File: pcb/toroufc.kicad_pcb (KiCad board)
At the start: 2 copper layers, 41.9 x 53.7 mm, 73 parts, among them J1 Conn_01x16_Male, J2 Conn_01x16_Male, J3 Conn_01x16_Male, J4 Conn_01x16_Male, J5 Conn_01x16_Male, J6 Conn_01x16_Male, J7 Conn_01x16_Male, J8 Conn_01x16_Male, J9 Conn_01x16_Male

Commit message: Moving stuff.
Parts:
- removed D57, D58, D59, D60, D61, D62, D63, D64: D, Diode_SMD:D_SOD-123
- removed J1, J2: Conn_01x16_Male, Connector_PinHeader_2.54mm:PinHeader_1x16_P2.54mm_Vertical
- added U1: YAAJ_BluePill, bluepill:YAAJ_BluePill_1, F.Cu at (101.0, 71.0)
- J3, J4, J5, J6, J7, J8, J9: moved to F.Cu
- moved D50 1062.6 mm to (116.7, 127.4), turned to 0 degrees
- moved D41 1058.6 mm to (105.2, 127.4), turned to 0 degrees
- moved D56 1056.7 mm to (110.9, 124.0), turned to 0 degrees
- moved D43 1056.7 mm to (110.9, 127.4), turned to 0 degrees
- moved D42 1055.4 mm to (99.4, 124.0), turned to 0 degrees
- moved D48 1050.1 mm to (116.7, 124.0), turned to 0 degrees
- moved D25 1045.3 mm to (128.2, 129.0), turned to 0 degrees
- moved D47 1044.9 mm to (123.6, 119.0), turned to 0 degrees
- moved D54 1043.7 mm to (135.1, 112.2), turned to 0 degrees
- moved D31 1043.5 mm to (99.4, 127.4), turned to 0 degrees
- moved D44 1043.0 mm to (123.6, 115.6), turned to 0 degrees
- moved D28 1042.7 mm to (122.4, 127.4), turned to 0 degrees
- moved D46 1041.5 mm to (129.3, 115.6), turned to 0 degrees
- moved D30 1040.1 mm to (105.2, 124.0), turned to 0 degrees
- moved D45 1038.6 mm to (129.3, 112.2), turned to 0 degrees
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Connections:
- net Net-(D1-Pad1) renamed /ROW8
- net Net-(D10-Pad1) renamed /ROW7
- net Net-(D11-Pad1) renamed /ROW6
- net Net-(D12-Pad1) renamed /ROW5
- net Net-(D13-Pad1) renamed /ROW4
- net Net-(D14-Pad1) renamed /ROW3
- net Net-(D15-Pad1) renamed /ROW2
- net Net-(D16-Pad1) renamed /ROW1
- net Net-(J1-Pad2) renamed /COL1
- net Net-(J1-Pad3) renamed /COL2
- net Net-(J1-Pad4) renamed /COL3
- net Net-(J1-Pad5) renamed /COL4
- net Net-(J1-Pad6) renamed /COL5
- net Net-(J1-Pad7) renamed /COL6
- net Net-(J1-Pad8) renamed /COL7
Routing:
- net Net-(J1-Pad1): track 93.6 -> 0.00 mm, vias 1 -> 0
- net /COL1: track 88.5 -> 0.00 mm, vias 1 -> 0
- net /COL2: track 85.1 -> 0.00 mm, vias 1 -> 0
- net /COL3: track 81.6 -> 0.00 mm, vias 1 -> 0
- net /COL4: track 78.0 -> 0.00 mm, vias 1 -> 0
- net /COL5: track 74.3 -> 0.00 mm, vias 1 -> 0
- net /COL6: track 71.0 -> 0.00 mm, vias 1 -> 0
- net /COL7: track 65.7 -> 0.00 mm
- net /ROW1: track 64.6 -> 0.00 mm
- net /ROW2: track 62.1 -> 0.00 mm
- net /ROW3: track 59.5 -> 0.00 mm
- net /ROW4: track 57.0 -> 0.00 mm
- net /ROW5: track 54.7 -> 0.00 mm
- net /ROW6: track 51.9 -> 0.00 mm
- net /ROW7: track 50.0 -> 0.00 mm
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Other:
- board outline removed
- net class Default removed
- rule pad_to_mask_clearance: 0.051 -> 0

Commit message: Starting with the PCB.
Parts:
- removed D23, D24, D25, D26, D27, D28, D29, D30, D31, D32, D33, D34, D35, D36, D37, D38, D39, D40, D41, D42, D43, D44, D45, D46, D47, D48, D49, D50, D51, D52, D53, D54, D55, D56: D, Diode_SMD:D_SOD-123
- added J1: HAT, Connector_PinHeader_2.54mm:PinHeader_1x06_P2.54mm_Vertical, F.Cu at (66.7, 67.3)
- added J10: RPAD, Connector_PinHeader_2.54mm:PinHeader_1x06_P2.54mm_Vertical, F.Cu at (102.9, 111.8)
- added J11: POT1-3, Connector_PinHeader_2.54mm:PinHeader_1x09_P2.54mm_Vertical, F.Cu at (114.3, 96.5)
- added J12: POT4-6, Connector_PinHeader_2.54mm:PinHeader_1x09_P2.54mm_Vertical, F.Cu at (121.9, 96.5)
- added J13: REN1, Connector_PinHeader_2.54mm:PinHeader_1x05_P2.54mm_Vertical, F.Cu at (78.7, 32.4)
- added J14: REN2, Connector_PinHeader_2.54mm:PinHeader_1x05_P2.54mm_Vertical, F.Cu at (97.2, 32.4)
- added J2: RKR1-2, Connector_PinHeader_2.54mm:PinHeader_1x06_P2.54mm_Vertical, F.Cu at (66.7, 44.5)
- J3: value Conn_01x16_Male -> RKR3-4; footprint Connector_PinHeader_2.54mm:PinHeader_1x16_P2.54mm_Vertical -> Connector_PinHeader_2.54mm:PinHeader_1x06_P2.54mm_Vertical
- J4: value Conn_01x16_Male -> LVR1-2; footprint Connector_PinHeader_2.54mm:PinHeader_1x16_P2.54mm_Vertical -> Connector_PinHeader_2.54mm:PinHeader_1x06_P2.54mm_Vertical
- J5: value Conn_01x16_Male -> MASTER-BIG1; footprint Connector_PinHeader_2.54mm:PinHeader_1x16_P2.54mm_Vertical -> Connector_PinHeader_2.54mm:PinHeader_1x06_P2.54mm_Vertical
- J6: value Conn_01x16_Male -> BIG2-3-4; footprint Connector_PinHeader_2.54mm:PinHeader_1x16_P2.54mm_Vertical -> Connector_PinHeader_2.54mm:PinHeader_1x06_P2.54mm_Vertical
- J7: value Conn_01x16_Male -> NPAD; footprint Connector_PinHeader_2.54mm:PinHeader_1x16_P2.54mm_Vertical -> Connector_PinHeader_2.54mm:PinHeader_1x10_P2.54mm_Vertical
- J8: value Conn_01x16_Male -> HPAD; footprint Connector_PinHeader_2.54mm:PinHeader_1x16_P2.54mm_Vertical -> Connector_PinHeader_2.54mm:PinHeader_1x08_P2.54mm_Vertical
- J9: value Conn_01x16_Male -> LPAD; footprint Connector_PinHeader_2.54mm:PinHeader_1x16_P2.54mm_Vertical -> Connector_PinHeader_2.54mm:PinHeader_1x06_P2.54mm_Vertical
- U1: value YAAJ_BluePill -> BluePill
- moved D19 110.7 mm to (79.4, 102.9), turned to 90 degrees
- moved D18 109.1 mm to (74.3, 102.9), turned to 90 degrees
- moved D20 105.0 mm to (69.2, 92.7), turned to 90 degrees
- moved D14 102.5 mm to (71.8, 59.7), turned to 90 degrees
- moved D1 99.8 mm to (67.9, 72.4), turned to 90 degrees
- moved D9 99.7 mm to (67.9, 82.5), turned to 90 degrees
- moved D16 95.5 mm to (79.4, 59.7), turned to 90 degrees
- moved D7 93.8 mm to (75.6, 49.5), turned to 90 degrees
- moved D3 92.4 mm to (75.6, 72.4), turned to 90 degrees
- moved D5 92.3 mm to (67.9, 49.5), turned to 90 degrees
- moved D2 90.7 mm to (71.8, 72.4), turned to 90 degrees
- moved D10 90.4 mm to (71.8, 82.5), turned to 90 degrees
- moved D6 90.2 mm to (71.8, 49.5), turned to 90 degrees
- moved D12 88.3 mm to (79.4, 82.5), turned to 90 degrees
- moved D8 87.8 mm to (79.4, 49.5), turned to 90 degrees
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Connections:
- D1 pad 1: /ROW8 -> /ROW5
- D10 pad 1: /ROW7 -> /ROW6
- D11 pad 1: /ROW6 -> /ROW7
- D12 pad 1: /ROW5 -> /ROW8
- D13 pad 1: /ROW4 -> /ROW1
- D14 pad 1: /ROW3 -> /ROW2
- D15 pad 1: /ROW2 -> /ROW3
- D16 pad 1: /ROW1 -> /ROW4
- D17 pad 1: /ROW8 -> /ROW6
- D19 pad 1: /ROW6 -> /ROW4
- D2 pad 1: /ROW7 -> /ROW6
- D2 pad 2: Net-(D2-Pad2) -> Net-(J1-Pad3)
- D21 pad 1: /ROW4 -> /ROW6
- D22 pad 1: /ROW3 -> /ROW7
- D3 pad 1: /ROW6 -> /ROW7
- D4 pad 1: /ROW5 -> /ROW8
- D5 pad 1: /ROW4 -> /ROW1
- D6 pad 1: /ROW3 -> /ROW2
- D7 pad 1: /ROW2 -> /ROW3
- D8 pad 1: /ROW1 -> /ROW4
- D9 pad 1: /ROW8 -> /ROW5
- J3 pad 1: Net-(D56-Pad2) -> /COL6
- J3 pad 2: /COL1 -> Net-(D9-Pad2)
- J3 pad 3: Net-(D55-Pad2) -> Net-(D10-Pad2)
- J3 pad 4: /COL1 -> /COL6
- J3 pad 5: Net-(D54-Pad2) -> Net-(D11-Pad2)
- J3 pad 6: /COL1 -> Net-(D12-Pad2)
- J4 pad 1: Net-(D48-Pad2) -> /COL7
- J4 pad 2: /COL2 -> Net-(D13-Pad2)
- J4 pad 3: Net-(D47-Pad2) -> Net-(D14-Pad2)
- J4 pad 4: /COL2 -> /COL7
- J4 pad 5: Net-(D46-Pad2) -> Net-(D15-Pad2)
- J4 pad 6: /COL2 -> Net-(D16-Pad2)
- J5 pad 1: Net-(D40-Pad2) -> /COL5
- J5 pad 2: /COL3 -> Net-(D17-Pad2)
- J5 pad 3: Net-(D39-Pad2) -> /COL5
- J5 pad 4: /COL3 -> Net-(D18-Pad2)
- J5 pad 5: Net-(D38-Pad2) -> /COL3
- J5 pad 6: /COL3 -> Net-(D19-Pad2)
- J6 pad 1: Net-(D32-Pad2) -> /COL3
- J6 pad 2: /COL4 -> Net-(D20-Pad2)
- J6 pad 3: Net-(D31-Pad2) -> /COL3
- J6 pad 4: /COL4 -> Net-(D21-Pad2)
- J6 pad 5: Net-(D30-Pad2) -> /COL3
- J6 pad 6: /COL4 -> Net-(D22-Pad2)
- J7 pad 1: Net-(D24-Pad2) -> /COL2
- J7 pad 10: /COL5 -> /ROW8
- J7 pad 2: /COL5 -> /COL3
- J7 pad 3: Net-(D23-Pad2) -> /ROW1
- J7 pad 4: /COL5 -> /ROW2
- J7 pad 5: Net-(D22-Pad2) -> /ROW3
- J7 pad 6: /COL5 -> /ROW4
- J7 pad 7: Net-(D21-Pad2) -> /ROW5
- J7 pad 8: /COL5 -> /ROW6
- J7 pad 9: Net-(D20-Pad2) -> /ROW7
- J8 pad 1: Net-(D16-Pad2) -> /COL1
- J8 pad 2: /COL6 -> /ROW1
- J8 pad 3: Net-(D15-Pad2) -> /ROW2
- J8 pad 4: /COL6 -> /ROW3
- J8 pad 5: Net-(D14-Pad2) -> /ROW4
- J8 pad 6: /COL6 -> /ROW5
- J8 pad 7: Net-(D13-Pad2) -> /ROW6
- J8 pad 8: /COL6 -> /ROW7
- J9 pad 1: Net-(D8-Pad2) -> /COL4
- J9 pad 2: /COL7 -> /ROW1
- J9 pad 3: Net-(D7-Pad2) -> /ROW2
- J9 pad 4: /COL7 -> /ROW3
- J9 pad 5: Net-(D6-Pad2) -> /ROW4
- J9 pad 6: /COL7 -> /ROW5
- U1 pad 1: unconnected-(U1-Pad1) -> /REN1C
- U1 pad 10: /COL5 -> /COL4
- U1 pad 11: /COL4 -> /COL3
- U1 pad 12: /COL3 -> /COL2
- U1 pad 13: /COL2 -> /COL1
- U1 pad 14: unconnected-(U1-Pad14) -> /SCL
- U1 pad 15: /COL1 -> /SDA
- U1 pad 18: unconnected-(U1-Pad18) -> /Vusb
- U1 pad 19: unconnected-(U1-Pad19) -> GND
- U1 pad 2: unconnected-(U1-Pad2) -> /REN1D
- U1 pad 20: unconnected-(U1-Pad20) -> VCC
- U1 pad 23: unconnected-(U1-Pad23) -> /REN2SW
- U1 pad 24: unconnected-(U1-Pad24) -> /REN1SW
- U1 pad 25: unconnected-(U1-Pad25) -> /POT3
- U1 pad 26: unconnected-(U1-Pad26) -> /POT2
- U1 pad 27: unconnected-(U1-Pad27) -> /POT1
- U1 pad 28: unconnected-(U1-Pad28) -> /POT4
- U1 pad 29: unconnected-(U1-Pad29) -> /POT5
- U1 pad 3: unconnected-(U1-Pad3) -> /REN2C
- U1 pad 30: unconnected-(U1-Pad30) -> /POT6
- U1 pad 38: unconnected-(U1-Pad38) -> VCC
- U1 pad 39: unconnected-(U1-Pad39) -> GND
- U1 pad 4: unconnected-(U1-Pad4) -> /REN2D
- U1 pad 40: unconnected-(U1-Pad40) -> GND
- U1 pad 5: unconnected-(U1-Pad5) -> /COL7
- U1 pad 6: /COL7 -> /COL6
- U1 pad 7: /COL6 -> /COL5
- U1 pad 8: unconnected-(U1-Pad8) -> /USBD-
- U1 pad 9: unconnected-(U1-Pad9) -> /USBD+
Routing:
- net VCC: track 0.00 -> 192.5 mm
- net /ROW3: track 0.00 -> 178.5 mm
- net GND: track 0.00 -> 147.5 mm
- net /ROW5: track 0.00 -> 128.4 mm, vias 0 -> 3
- net /ROW6: track 0.00 -> 124.5 mm
- net /ROW1: track 0.00 -> 123.6 mm, vias 0 -> 2
- net /ROW4: track 0.00 -> 120.5 mm, vias 0 -> 1
- net /COL3: track 0.00 -> 110.6 mm, vias 0 -> 1
- net /COL6: track 0.00 -> 86.0 mm
- net /REN1SW: track 0.00 -> 79.9 mm, vias 0 -> 2
- net /ROW7: track 0.00 -> 72.0 mm
- net /REN2SW: track 0.00 -> 71.0 mm, vias 0 -> 1
- net /ROW2: track 0.00 -> 66.3 mm
- net /ROW8: track 0.00 -> 63.5 mm, vias 0 -> 1
- net /COL4: track 0.00 -> 59.1 mm, vias 0 -> 1
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
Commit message: First PCB that passes DRC
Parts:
- added J15: I2C, Connector_PinHeader_2.54mm:PinHeader_1x04_P2.54mm_Vertical, F.Cu at (95.0, 111.8)
- added J16: Conn_01x04_Male, Connector_PinHeader_2.54mm:PinHeader_1x04_P2.54mm_Vertical, F.Cu at (119.8, 111.8)
- moved J7 43.2 mm to (64.3, 111.7), turned to 90 degrees
- moved J13 39.0 mm to (114.3, 48.4), turned to 0 degrees
- moved J10 37.1 mm to (66.9, 120.8), turned to 90 degrees
- moved J8 36.1 mm to (66.9, 116.4), turned to 90 degrees
- moved J14 29.4 mm to (121.8, 48.4), turned to 0 degrees
- moved J9 15.5 mm to (104.7, 120.8)
- moved D10 0.81 mm to (71.2, 83.2)
- moved D11 0.81 mm to (75.1, 83.2)
- moved D12 0.81 mm to (78.9, 83.2)
- moved D20 0.81 mm to (68.7, 93.3)
- moved D21 0.81 mm to (73.8, 93.3)
- moved D22 0.81 mm to (78.9, 93.3)
- moved J6 0.81 mm to (66.2, 88.3)
- moved D14 0.81 mm to (71.2, 60.3)
- moved D15 0.81 mm to (75.1, 60.3)
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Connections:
- D19 pad 1: /ROW4 -> /ROW5
- D20 pad 1: /ROW5 -> /ROW6
- D21 pad 1: /ROW6 -> /ROW7
- D22 pad 1: /ROW7 -> /ROW8
- U1 pad 31: /ROW1 -> /ROW5
- U1 pad 32: /ROW2 -> /ROW6
- U1 pad 33: /ROW3 -> /ROW4
- U1 pad 34: /ROW4 -> /ROW3
- U1 pad 35: /ROW5 -> /ROW2
- U1 pad 36: /ROW6 -> /ROW1
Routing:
- net /ROW2: track 66.3 -> 167.1 mm
- net /COL2: track 0.00 -> 62.8 mm
- net /USBD-: track 0.00 -> 56.4 mm, vias 0 -> 1
- net /COL4: track 59.1 -> 114.5 mm, vias 1 -> 0
- net /Vusb: track 0.00 -> 54.5 mm
- net /USBD+: track 0.00 -> 52.8 mm, vias 0 -> 1
- net /COL1: track 0.00 -> 49.6 mm
- net /ROW1: track 123.6 -> 172.5 mm, vias 2 -> 0
- net /COL3: track 110.6 -> 72.5 mm, vias 1 -> 0
- net /ROW4: track 120.5 -> 157.4 mm, vias 1 -> 0
- net /SCL: track 0.00 -> 35.1 mm
- net /COL5: track 57.7 -> 90.3 mm, vias 0 -> 1
- net /SDA: track 0.00 -> 31.5 mm
- net GND: track 147.5 -> 178.3 mm
- net /ROW8: track 63.5 -> 83.9 mm, vias 1 -> 0
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- added copper zone on B.Cu, net GND
- added copper zone on F.Cu, net VCC
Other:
- board outline added: 70.5 x 87.5 mm

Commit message: Main PCB looking good.
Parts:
- moved D10 52.1 mm to (122.5, 92.4)
- moved D14 52.1 mm to (122.5, 69.6)
- moved D2 52.1 mm to (122.5, 82.3)
- moved D6 52.1 mm to (122.5, 59.4)
- moved D1 52.1 mm to (118.7, 82.3)
- moved D11 52.1 mm to (126.4, 92.4)
- moved D12 52.1 mm to (130.2, 92.4)
- moved D13 52.1 mm to (118.7, 69.6)
- moved D15 52.1 mm to (126.4, 69.6)
- moved D16 52.1 mm to (130.2, 69.6)
- moved D17 52.1 mm to (120.0, 112.8)
- moved D18 52.1 mm to (125.1, 112.8)
- moved D19 52.1 mm to (130.2, 112.8)
- moved D20 52.1 mm to (120.0, 102.6)
- moved D21 52.1 mm to (125.1, 102.6)
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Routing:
- net VCC: track 173.3 -> 105.9 mm, vias 1 -> 0
- net /USBD+: track 52.8 -> 60.9 mm
- net /USBD-: track 56.4 -> 61.1 mm
- net /POT3: track 14.8 -> 13.3 mm
- net /REN1SW: track 74.6 -> 73.4 mm
- net /POT6: track 41.8 -> 42.6 mm
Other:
- board size 70.5 x 87.5 mm -> 70 x 87 mm
- board text added: "+"
- board text added: "CLK"
- board text added: "DT"
- board text added: "E"
- board text added: "GND"
- board text added: "HAT: C"
- board text added: "HPAD"
- board text added: "LPAD"
- board text added: "N"
- board text added: "NPAD"
- board text added: "POT1"
- board text added: "POT2"
- board text added: "POT3"
- board text added: "POT4"
- board text added: "POT5"
- board text added: "POT6"
- board text added: "RKR: common / up / down LVR: common / up / down"
- board text added: "ROT1"
- board text added: "ROT2"
- board text added: "RPAD"
- board text added: "S"
- board text added: "SCL"
- board text added: "SDA"
- board text added: "SW"
- board text added: "Toro-UFC v1"
- board text added: "USBD+"
- board text added: "USBD-"
- board text added: "VCC"
- board text added: "Vusb"
- board text added: "W"
- board text added: "| A/A | A/G | BIG1 |"
- board text added: "| BIG2 | BIG3 | BIG4 |"
- board text added: "| LVR1 | LVR2 |"
- board text added: "| RKR1 | RKR2 |"
- board text added: "| RKR3 | RKR4 |"

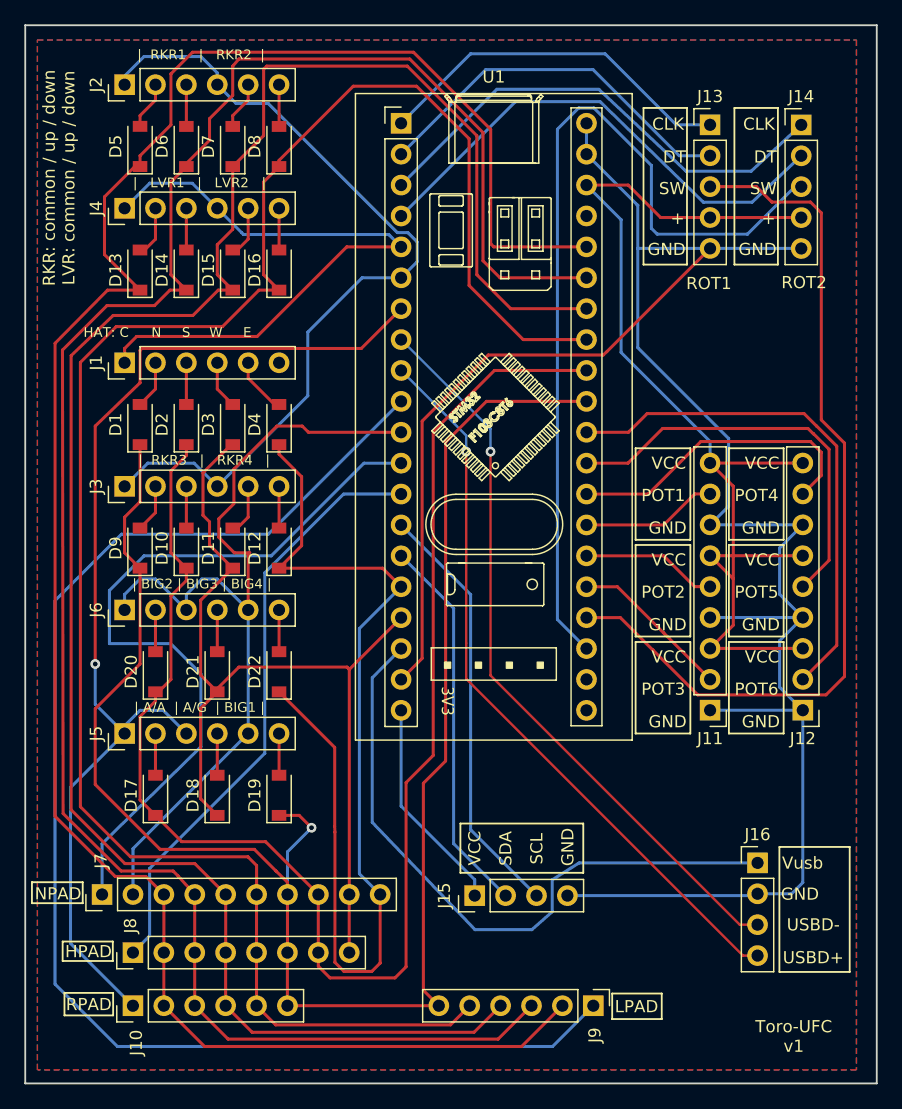
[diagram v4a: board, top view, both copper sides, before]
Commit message: Add mounting holes to pcb.
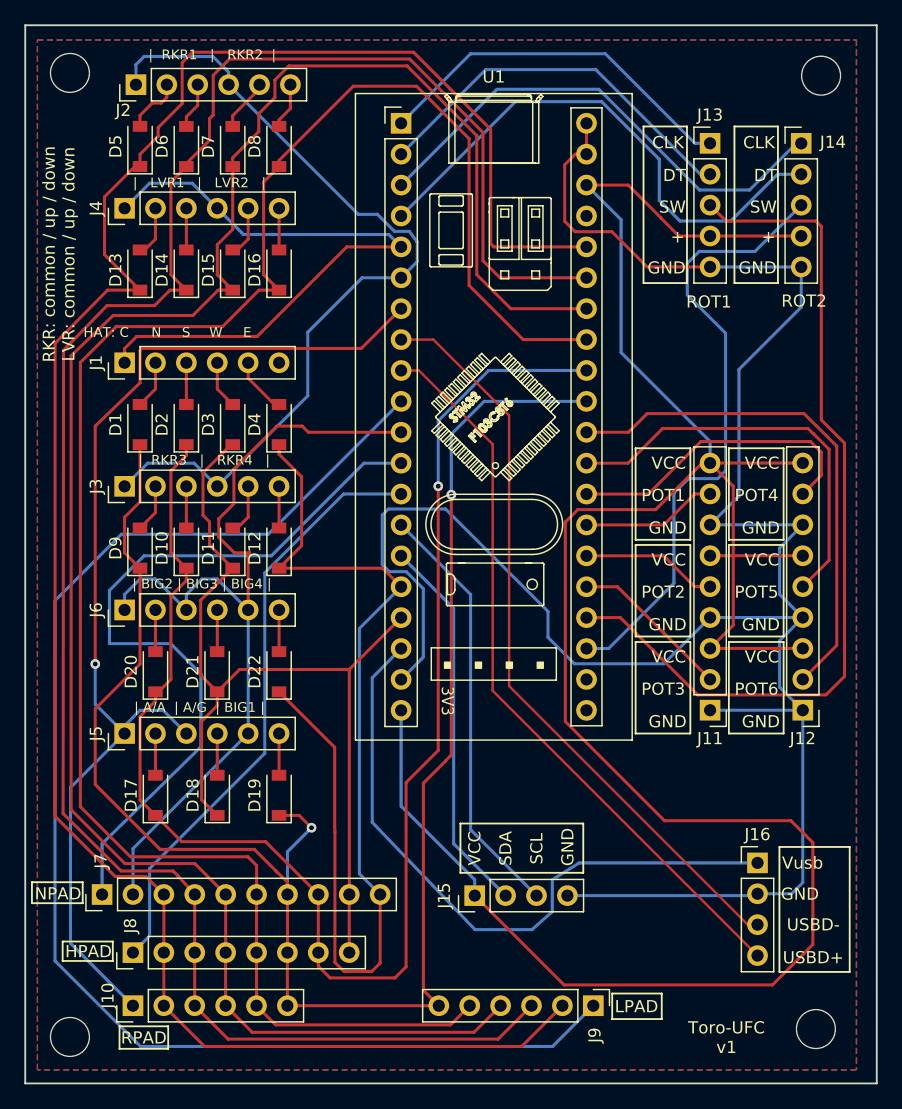
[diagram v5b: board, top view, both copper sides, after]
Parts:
- added REF**: MountingHole_3.2mm_M3, MountingHole:MountingHole_3.2mm_M3, F.Cu at (174.7, 53.6)
- added REF**: MountingHole_3.2mm_M3, MountingHole:MountingHole_3.2mm_M3, F.Cu at (113.0, 53.4)
- added REF**: MountingHole_3.2mm_M3, MountingHole:MountingHole_3.2mm_M3, F.Cu at (174.3, 132.0)
- added REF**: MountingHole_3.2mm_M3, MountingHole:MountingHole_3.2mm_M3, F.Cu at (113.0, 132.6)
- moved J14 1.52 mm to (173.1, 59.2)
- moved J13 1.52 mm to (165.6, 59.2)
- moved J2 0.93 mm to (118.4, 54.3)
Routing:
- net VCC: track 105.9 -> 199.3 mm
- net /REN2SW: track 73.4 -> 51.5 mm
- net GND: track 178.7 -> 181.6 mm
- net /REN2D: track 41.7 -> 44.4 mm
- net /REN1SW: track 73.4 -> 72.1 mm
- net /USBD-: track 61.1 -> 62.3 mm, vias 1 -> 0
- net /COL4: track 114.5 -> 113.4 mm
- net /ROW3: track 163.8 -> 162.8 mm
- net /REN2C: track 40.3 -> 41.2 mm
- net Net-(D5-Pad2): track 3.96 -> 4.77 mm
- net /REN1D: track 31.2 -> 31.8 mm
- net /REN1C: track 30.2 -> 30.8 mm
- net /ROW6: track 123.4 -> 123.6 mm, vias 0 -> 1
- net /USBD+: track 60.9 -> 61.1 mm, vias 1 -> 0
- net /ROW5: track 142.2 -> 142.3 mm, vias 1 -> 2
